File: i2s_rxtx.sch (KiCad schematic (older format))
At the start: 12 parts

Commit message: -- update
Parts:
- added C6, C8: 100nF, Capacitor_SMD:C_0805_2012Metric_Pad1.15x1.40mm_HandSolder, symbol agg:C
- added C7, C9: 10nF, Capacitor_SMD:C_0805_2012Metric_Pad1.15x1.40mm_HandSolder, symbol agg:C
- added IC2, IC3: AM26C31, agg:SOIC-16, symbol agg:AM26C31
- added J3: CONN_01x05, Connector_PinHeader_2.00mm:PinHeader_1x05_P2.00mm_Vertical, symbol agg:CONN_01x05
- added J4, J5: RJ45_Shielded, agg:RJ45_Weidmueller, symbol Connector:RJ45_Shielded
- C1: renamed from C?; footprint (none) -> Capacitor_SMD:CP_Elec_6.3x5.4
- C2, C3, C4, C5: renamed from C?; footprint (none) -> Capacitor_SMD:C_0805_2012Metric_Pad1.15x1.40mm_HandSolder
- J1: renamed from J?; footprint (none) -> Connector_PinHeader_2.00mm:PinHeader_1x02_P2.00mm_Vertical
- J2: renamed from J?; footprint (none) -> agg:RJ45_Weidmueller
- R1, R2, R4: renamed from R?; footprint (none) -> Resistor_SMD:R_1206_3216Metric_Pad1.42x1.75mm_HandSolder
- R3: renamed from R?; value 10=R -> 100R; footprint (none) -> Resistor_SMD:R_1206_3216Metric_Pad1.42x1.75mm_HandSolder
- gave numbers to parts that had none: 1
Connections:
- net +5V: now also C6.1, C7.1, C8.1, C9.1, IC2.16 (VCC), IC3.16 (VCC)
- net GND: now also C4.2, C5.2, IC1.8 (GND), C6.2, C7.2, C8.2, C9.2, IC2.12 (~G), IC2.4 (G), IC2.8 (GND), IC3.12 (~G), IC3.4 (G), IC3.8 (GND), J3.1, J4.SH, J5.SH
- net I2S_CH12: now also IC2.9 (3A), IC3.9 (3A), J3.4
- net I2S_CH34: now also IC2.15 (4A), IC3.15 (4A), J3.5
- net I2S_CLK: now also IC2.7 (2A), IC3.7 (2A), J3.3
- net I2S_WS: now also IC2.1 (1A), IC3.1 (1A), J3.2
- new net: IC2.10 (3Y), J4.5
- new net: IC2.11 (3Z), J4.6
- new net: IC2.13 (4Z), J4.8
- new net: IC2.14 (4Y), J4.7
- new net: IC2.2 (1Y), J4.1
- new net: IC2.3 (1Z), J4.2
- new net: IC2.5 (2Z), J4.4
- new net: IC2.6 (2Y), J4.3
- new net: IC3.10 (3Y), J5.5
- new net: IC3.11 (3Z), J5.6
- new net: IC3.13 (4Z), J5.8
- new net: IC3.14 (4Y), J5.7
- new net: IC3.2 (1Y), J5.1
- new net: IC3.3 (1Z), J5.2
- new net: IC3.5 (2Z), J5.4
- new net: IC3.6 (2Y), J5.3

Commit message: --update
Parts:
- added R5, R6, R7, R8: 500K, Resistor_SMD:R_0805_2012Metric_Pad1.15x1.40mm_HandSolder, symbol agg:R
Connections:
- net GND: now also R5.2, R6.2, R7.2, R8.2
- net I2S_CH12: now also R6.1
- net I2S_CH34: now also R5.1
- net I2S_CLK: now also R7.1
- net I2S_WS: now also R8.1
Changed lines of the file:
@@
 Text GLabel 2600 3400 0    50   Input ~ 0
 CH_34_Z
-Wire Wire Line
-	3450 1800 3500 1800
-Wire Wire Line
-	3450 2000 3500 2000
-Wire Wire Line
-	3450 2200 3500 2200
-Wire Wire Line
-	3450 2400 3500 2400
-Text GLabel 3500 1800 2    50   Input ~ 0
+Text GLabel 3950 1800 2    50   Input ~ 0
 I2S_WS
-Text GLabel 3500 2000 2    50   Input ~ 0
+Text GLabel 3950 2000 2    50   Input ~ 0
 I2S_CLK
-Text GLabel 3500 2200 2    50   Input ~ 0
+Text GLabel 3950 2200 2    50   Input ~ 0
 I2S_CH12
-Text GLabel 3500 2400 2    50   Input ~ 0
+Text GLabel 3950 2400 2    50   Input ~ 0
 I2S_CH34
 Wire Wire Line
@@
 $EndComp
 $Comp
-L power:GND #PWR?
+L power:GND #PWR0111
 U 1 1 5D0BFC09
 P 1050 2950
-F 0 "#PWR?" H 1050 2700 50  0001 C CNN
+F 0 "#PWR0111" H 1050 2700 50  0001 C CNN
 F 1 "GND" H 1055 2777 50  0000 C CNN
 F 2 "" H 1050 2950 50  0001 C CNN
@@
 Wire Wire Line
 	1050 2850 1050 2950
+$Comp
+L agg:R R5
+U 1 1 5D069D45
+P 3500 2450
+F 0 "R5" V 3504 2494 50  0000 L CNN
+F 1 "500K" V 3595 2494 50  0000 L CNN
+F 2 "Resistor_SMD:R_0805_2012Metric_Pad1.15x1.40mm_HandSolder" H 3500 2450 50  0001 C CNN
+F 3 "" H 3500 2450 50  0001 C CNN
+	1    3500 2450
+	0    1    1    0
+$EndComp
+$Comp
+L agg:R R6
+U 1 1 5D06AB9A
+P 3600 2250
+F 0 "R6" V 3604 2294 50  0000 L CNN
+F 1 "500K" V 3695 2294 50  0000 L CNN
+F 2 "Resistor_SMD:R_0805_2012Metric_Pad1.15x1.40mm_HandSolder" H 3600 2250 50  0001 C CNN
+F 3 "" H 3600 2250 50  0001 C CNN
+	1    3600 2250
+	0    1    1    0
+$EndComp
+$Comp
+L agg:R R7
+U 1 1 5D06B197
+P 3700 2050
+F 0 "R7" V 3704 2094 50  0000 L CNN
+F 1 "500K" V 3795 2094 50  0000 L CNN
+F 2 "Resistor_SMD:R_0805_2012Metric_Pad1.15x1.40mm_HandSolder" H 3700 2050 50  0001 C CNN
+F 3 "" H 3700 2050 50  0001 C CNN
+	1    3700 2050
+	0    1    1    0
+$EndComp
+$Comp
+L agg:R R8
+U 1 1 5D06B744
+P 3800 1850
+F 0 "R8" V 3804 1894 50  0000 L CNN
+F 1 "500K" V 3895 1894 50  0000 L CNN
+F 2 "Resistor_SMD:R_0805_2012Metric_Pad1.15x1.40mm_HandSolder" H 3800 1850 50  0001 C CNN
+F 3 "" H 3800 1850 50  0001 C CNN
+	1    3800 1850
+	0    1    1    0
+$EndComp
+Wire Wire Line
+	3450 1800 3800 1800
+Wire Wire Line
+	3800 1800 3950 1800
+Connection ~ 3800 1800
+Wire Wire Line
+	3600 2600 3500 2600
+Connection ~ 3600 2600
+$Comp
+L power:GND #PWR0112
+U 1 1 5D0A366B
+P 3600 2700
+F 0 "#PWR0112" H 3600 2450 50  0001 C CNN
+F 1 "GND" H 3605 2527 50  0000 C CNN
+F 2 "" H 3600 2700 50  0001 C CNN
+F 3 "" H 3600 2700 50  0001 C CNN
+	1    3600 2700
+	1    0    0    -1
+$EndComp
+Wire Wire Line
+	3600 2600 3600 2700
+Wire Wire Line
+	3600 2600 3700 2600
+Wire Wire Line
+	3800 1800 3800 1850
+Wire Wire Line
+	3450 2400 3500 2400
+Wire Wire Line
+	3450 2000 3700 2000
+Wire Wire Line
+	3450 2200 3600 2200
+Wire Wire Line
+	3700 2000 3700 2050
+Connection ~ 3700 2000
+Wire Wire Line
+	3700 2000 3950 2000
+Wire Wire Line
+	3600 2200 3600 2250
+Connection ~ 3600 2200
+Wire Wire Line
+	3600 2200 3950 2200
+Wire Wire Line
+	3500 2400 3500 2450
+Connection ~ 3500 2400
+Wire Wire Line
+	3500 2400 3950 2400
+Wire Wire Line
+	3500 2550 3500 2600
+Wire Wire Line
+	3600 2350 3600 2600
+Wire Wire Line
+	3700 2150 3700 2600
+Connection ~ 3700 2600
+Wire Wire Line
+	3700 2600 3800 2600
+Wire Wire Line
+	3800 1950 3800 2600
 $EndSCHEMATC

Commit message: -- added mounting holes
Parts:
- added H1, H2, H3, H4: MountingHole, MountingHole:MountingHole_3.2mm_M3_Pad, symbol Mechanical:MountingHole
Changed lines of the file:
@@
 Wire Wire Line
 	3800 1950 3800 2600
+$Comp
+L Mechanical:MountingHole H1
+U 1 1 5D0E85FD
+P 850 3500
+F 0 "H1" H 950 3546 50  0000 L CNN
+F 1 "MountingHole" H 950 3455 50  0000 L CNN
+F 2 "MountingHole:MountingHole_3.2mm_M3_Pad" H 850 3500 50  0001 C CNN
+F 3 "~" H 850 3500 50  0001 C CNN
+	1    850  3500
+	1    0    0    -1
+$EndComp
+$Comp
+L Mechanical:MountingHole H2
+U 1 1 5D0E907F
+P 850 3700
+F 0 "H2" H 950 3746 50  0000 L CNN
+F 1 "MountingHole" H 950 3655 50  0000 L CNN
+F 2 "MountingHole:MountingHole_3.2mm_M3_Pad" H 850 3700 50  0001 C CNN
+F 3 "~" H 850 3700 50  0001 C CNN
+	1    850  3700
+	1    0    0    -1
+$EndComp
+$Comp
+L Mechanical:MountingHole H3
+U 1 1 5D0E92F0
+P 850 3900
+F 0 "H3" H 950 3946 50  0000 L CNN
+F 1 "MountingHole" H 950 3855 50  0000 L CNN
+F 2 "MountingHole:MountingHole_3.2mm_M3_Pad" H 850 3900 50  0001 C CNN
+F 3 "~" H 850 3900 50  0001 C CNN
+	1    850  3900
+	1    0    0    -1
+$EndComp
+$Comp
+L Mechanical:MountingHole H4
+U 1 1 5D0E9AAA
+P 850 4100
+F 0 "H4" H 950 4146 50  0000 L CNN
+F 1 "MountingHole" H 950 4055 50  0000 L CNN
+F 2 "MountingHole:MountingHole_3.2mm_M3_Pad" H 850 4100 50  0001 C CNN
+F 3 "~" H 850 4100 50  0001 C CNN
+	1    850  4100
+	1    0    0    -1
+$EndComp
 $EndSCHEMATC

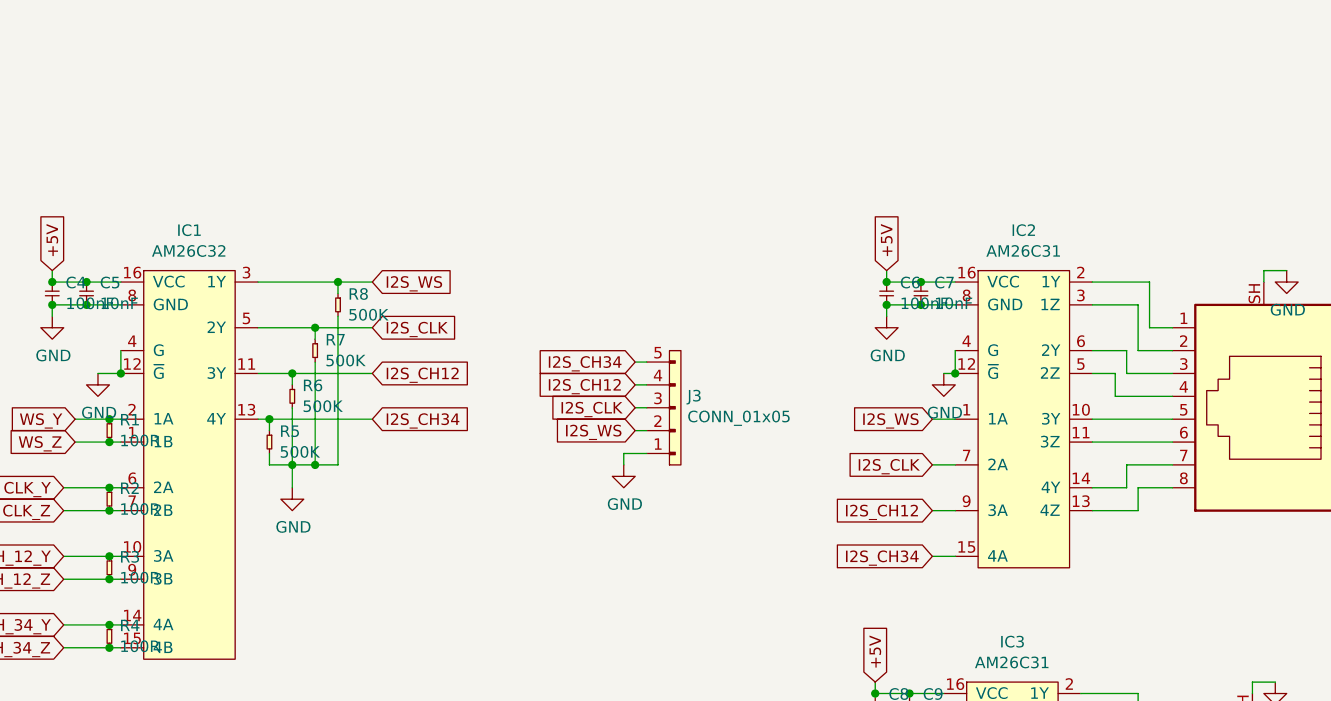
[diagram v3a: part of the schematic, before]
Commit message: -- added voltage divider for 3.3V outputs
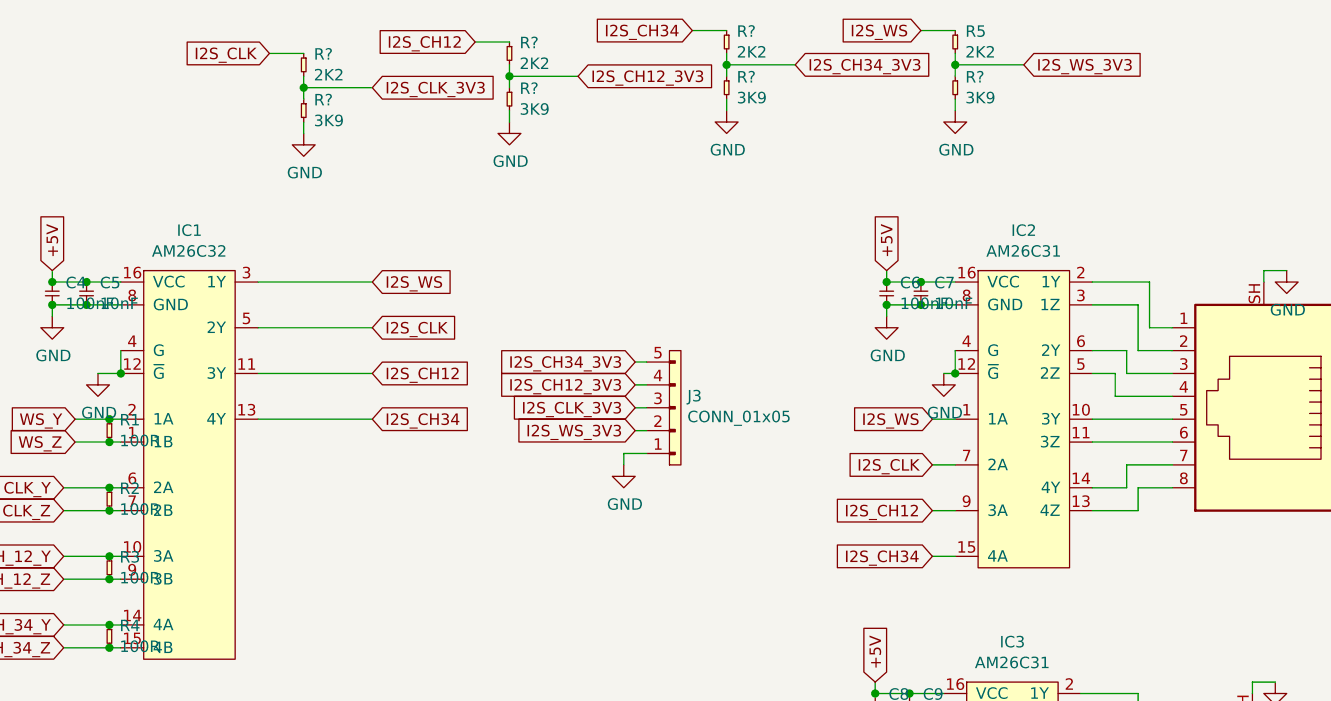
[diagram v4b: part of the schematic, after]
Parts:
- removed R6, R7, R8: 500K, Resistor_SMD:R_0805_2012Metric_Pad1.15x1.40mm_HandSolder, symbol agg:R
- added R? (x4): 3K9, Resistor_SMD:R_0805_2012Metric_Pad1.15x1.40mm_HandSolder, symbol agg:R
- added R? (x3): 2K2, Resistor_SMD:R_0805_2012Metric_Pad1.15x1.40mm_HandSolder, symbol agg:R
- R5: value 500K -> 2K2
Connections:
- net GND: now also R?.2, R?.2, R?.2, R?.2; no longer R5.2
- net I2S_CH12: now also R?.1; no longer J3.4
- net I2S_CH34: now also R?.1; no longer J3.5, R5.1
- net I2S_CLK: now also R?.1; no longer J3.3
- net I2S_WS: now also R5.1; no longer J3.2
- new net I2S_CH12_3V3: J3.4, R?.1, R?.2
- new net I2S_CH34_3V3: J3.5, R?.1, R?.2
- new net I2S_CLK_3V3: J3.3, R?.1, R?.2
- new net I2S_WS_3V3: J3.2, R5.2, R?.1
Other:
- moved on the sheet: R5
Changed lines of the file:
@@
 	5050 2550 5150 2550
 Text GLabel 5100 2450 0    50   Input ~ 0
-I2S_WS
+I2S_WS_3V3
 Text GLabel 5100 2350 0    50   Input ~ 0
-I2S_CLK
+I2S_CLK_3V3
 Text GLabel 5100 2250 0    50   Input ~ 0
-I2S_CH12
+I2S_CH12_3V3
 Text GLabel 5100 2150 0    50   Input ~ 0
-I2S_CH34
+I2S_CH34_3V3
 Wire Wire Line
 	6200 1900 6200 1950
@@
 L agg:R R5
 U 1 1 5D069D45
-P 3500 2450
-F 0 "R5" V 3504 2494 50  0000 L CNN
-F 1 "500K" V 3595 2494 50  0000 L CNN
-F 2 "Resistor_SMD:R_0805_2012Metric_Pad1.15x1.40mm_HandSolder" H 3500 2450 50  0001 C CNN
-F 3 "" H 3500 2450 50  0001 C CNN
-	1    3500 2450
-	0    1    1    0
-$EndComp
-$Comp
-L agg:R R6
-U 1 1 5D06AB9A
-P 3600 2250
-F 0 "R6" V 3604 2294 50  0000 L CNN
-F 1 "500K" V 3695 2294 50  0000 L CNN
-F 2 "Resistor_SMD:R_0805_2012Metric_Pad1.15x1.40mm_HandSolder" H 3600 2250 50  0001 C CNN
-F 3 "" H 3600 2250 50  0001 C CNN
-	1    3600 2250
-	0    1    1    0
-$EndComp
-$Comp
-L agg:R R7
-U 1 1 5D06B197
-P 3700 2050
-F 0 "R7" V 3704 2094 50  0000 L CNN
-F 1 "500K" V 3795 2094 50  0000 L CNN
-F 2 "Resistor_SMD:R_0805_2012Metric_Pad1.15x1.40mm_HandSolder" H 3700 2050 50  0001 C CNN
-F 3 "" H 3700 2050 50  0001 C CNN
-	1    3700 2050
-	0    1    1    0
-$EndComp
-$Comp
-L agg:R R8
-U 1 1 5D06B744
-P 3800 1850
-F 0 "R8" V 3804 1894 50  0000 L CNN
-F 1 "500K" V 3895 1894 50  0000 L CNN
-F 2 "Resistor_SMD:R_0805_2012Metric_Pad1.15x1.40mm_HandSolder" H 3800 1850 50  0001 C CNN
-F 3 "" H 3800 1850 50  0001 C CNN
-	1    3800 1850
-	0    1    1    0
-$EndComp
-Wire Wire Line
-	3450 1800 3800 1800
-Wire Wire Line
-	3800 1800 3950 1800
-Connection ~ 3800 1800
-Wire Wire Line
-	3600 2600 3500 2600
-Connection ~ 3600 2600
-$Comp
-L power:GND #PWR0112
-U 1 1 5D0A366B
-P 3600 2700
-F 0 "#PWR0112" H 3600 2450 50  0001 C CNN
-F 1 "GND" H 3605 2527 50  0000 C CNN
-F 2 "" H 3600 2700 50  0001 C CNN
-F 3 "" H 3600 2700 50  0001 C CNN
-	1    3600 2700
-	1    0    0    -1
-$EndComp
-Wire Wire Line
-	3600 2600 3600 2700
-Wire Wire Line
-	3600 2600 3700 2600
-Wire Wire Line
-	3800 1800 3800 1850
-Wire Wire Line
-	3450 2400 3500 2400
-Wire Wire Line
-	3450 2000 3700 2000
-Wire Wire Line
-	3450 2200 3600 2200
-Wire Wire Line
-	3700 2000 3700 2050
-Connection ~ 3700 2000
-Wire Wire Line
-	3700 2000 3950 2000
-Wire Wire Line
-	3600 2200 3600 2250
-Connection ~ 3600 2200
-Wire Wire Line
-	3600 2200 3950 2200
-Wire Wire Line
-	3500 2400 3500 2450
-Connection ~ 3500 2400
-Wire Wire Line
-	3500 2400 3950 2400
-Wire Wire Line
-	3500 2550 3500 2600
-Wire Wire Line
-	3600 2350 3600 2600
-Wire Wire Line
-	3700 2150 3700 2600
-Connection ~ 3700 2600
-Wire Wire Line
-	3700 2600 3800 2600
-Wire Wire Line
-	3800 1950 3800 2600
+P 6500 700
+F 0 "R5" V 6504 744 50  0000 L CNN
+F 1 "2K2" V 6595 744 50  0000 L CNN
+F 2 "Resistor_SMD:R_0805_2012Metric_Pad1.15x1.40mm_HandSolder" H 6500 700 50  0001 C CNN
+F 3 "" H 6500 700 50  0001 C CNN
+	1    6500 700
+	0    1    1    0
+$EndComp
 $Comp
 L Mechanical:MountingHole H1
@@
 	1    0    0    -1
 $EndComp
+Wire Wire Line
+	3450 2400 3950 2400
+Wire Wire Line
+	3450 2200 3950 2200
+Wire Wire Line
+	3450 2000 3950 2000
+Wire Wire Line
+	3450 1800 3950 1800
+Text GLabel 6350 700  0    50   Input ~ 0
+I2S_WS
+$Comp
+L agg:R R?
+U 1 1 5D540B22
+P 6500 900
+F 0 "R?" V 6504 944 50  0000 L CNN
+F 1 "3K9" V 6595 944 50  0000 L CNN
+F 2 "Resistor_SMD:R_0805_2012Metric_Pad1.15x1.40mm_HandSolder" H 6500 900 50  0001 C CNN
+F 3 "" H 6500 900 50  0001 C CNN
+	1    6500 900
+	0    1    1    0
+$EndComp
+$Comp
+L power:GND #PWR?
+U 1 1 5D54109E
+P 6500 1050
+F 0 "#PWR?" H 6500 800 50  0001 C CNN
+F 1 "GND" H 6505 877 50  0000 C CNN
+F 2 "" H 6500 1050 50  0001 C CNN
+F 3 "" H 6500 1050 50  0001 C CNN
+	1    6500 1050
+	1    0    0    -1
+$EndComp
+Wire Wire Line
+	6350 700  6500 700
+Wire Wire Line
+	6500 800  6500 850
+Text GLabel 6800 850  2    50   Input ~ 0
+I2S_WS_3V3
+Wire Wire Line
+	6800 850  6500 850
+Wire Wire Line
+	6500 1000 6500 1050
+Wire Wire Line
+	6500 900  6500 850
+Connection ~ 6500 850
+$Comp
+L agg:R R?
+U 1 1 5D56E9E4
+P 3650 800
+F 0 "R?" V 3654 844 50  0000 L CNN
+F 1 "2K2" V 3745 844 50  0000 L CNN
+F 2 "Resistor_SMD:R_0805_2012Metric_Pad1.15x1.40mm_HandSolder" H 3650 800 50  0001 C CNN
+F 3 "" H 3650 800 50  0001 C CNN
+	1    3650 800
+	0    1    1    0
+$EndComp
+Text GLabel 3500 800  0    50   Input ~ 0
+I2S_CLK
+$Comp
+L agg:R R?
+U 1 1 5D56E9EF
+P 3650 1000
+F 0 "R?" V 3654 1044 50  0000 L CNN
+F 1 "3K9" V 3745 1044 50  0000 L CNN
+F 2 "Resistor_SMD:R_0805_2012Metric_Pad1.15x1.40mm_HandSolder" H 3650 1000 50  0001 C CNN
+F 3 "" H 3650 1000 50  0001 C CNN
+	1    3650 1000
+	0    1    1    0
+$EndComp
+$Comp
+L power:GND #PWR?
+U 1 1 5D56E9F9
+P 3650 1150
+F 0 "#PWR?" H 3650 900 50  0001 C CNN
+F 1 "GND" H 3655 977 50  0000 C CNN
+F 2 "" H 3650 1150 50  0001 C CNN
+F 3 "" H 3650 1150 50  0001 C CNN
+	1    3650 1150
+	1    0    0    -1
+$EndComp
+Wire Wire Line
+	3500 800  3650 800
+Wire Wire Line
+	3650 900  3650 950
+Text GLabel 3950 950  2    50   Input ~ 0
+I2S_CLK_3V3
+Wire Wire Line
+	3950 950  3650 950
+Wire Wire Line
+	3650 1100 3650 1150
+Wire Wire Line
+	3650 1000 3650 950
+Connection ~ 3650 950
+$Comp
+L agg:R R?
+U 1 1 5D5754C4
+P 4550 750
+F 0 "R?" V 4554 794 50  0000 L CNN
+F 1 "2K2" V 4645 794 50  0000 L CNN
+F 2 "Resistor_SMD:R_0805_2012Metric_Pad1.15x1.40mm_HandSolder" H 4550 750 50  0001 C CNN
+F 3 "" H 4550 750 50  0001 C CNN
+	1    4550 750
+	0    1    1    0
+$EndComp
+Text GLabel 4400 750  0    50   Input ~ 0
+I2S_CH12
+$Comp
+L agg:R R?
+U 1 1 5D5754CF
+P 4550 950
+F 0 "R?" V 4554 994 50  0000 L CNN
+F 1 "3K9" V 4645 994 50  0000 L CNN
+F 2 "Resistor_SMD:R_0805_2012Metric_Pad1.15x1.40mm_HandSolder" H 4550 950 50  0001 C CNN
+F 3 "" H 4550 950 50  0001 C CNN
+	1    4550 950
+	0    1    1    0
+$EndComp
+$Comp
+L power:GND #PWR?
+U 1 1 5D5754D9
+P 4550 1100
+F 0 "#PWR?" H 4550 850 50  0001 C CNN
+F 1 "GND" H 4555 927 50  0000 C CNN
+F 2 "" H 4550 1100 50  0001 C CNN
+F 3 "" H 4550 1100 50  0001 C CNN
+	1    4550 1100
+	1    0    0    -1
+$EndComp
+Wire Wire Line
+	4400 750  4550 750
+Wire Wire Line
+	4550 850  4550 900
+Text GLabel 4850 900  2    50   Input ~ 0
+I2S_CH12_3V3
+Wire Wire Line
+	4850 900  4550 900
+Wire Wire Line
+	4550 1050 4550 1100
+Wire Wire Line
+	4550 950  4550 900
+Connection ~ 4550 900
+$Comp
+L agg:R R?
+U 1 1 5D57D61F
+P 5500 700
+F 0 "R?" V 5504 744 50  0000 L CNN
+F 1 "2K2" V 5595 744 50  0000 L CNN
+F 2 "Resistor_SMD:R_0805_2012Metric_Pad1.15x1.40mm_HandSolder" H 5500 700 50  0001 C CNN
+F 3 "" H 5500 700 50  0001 C CNN
+	1    5500 700
+	0    1    1    0
+$EndComp
+Text GLabel 5350 700  0    50   Input ~ 0
+I2S_CH34
+$Comp
+L agg:R R?
+U 1 1 5D57D62A
+P 5500 900
+F 0 "R?" V 5504 944 50  0000 L CNN
+F 1 "3K9" V 5595 944 50  0000 L CNN
+F 2 "Resistor_SMD:R_0805_2012Metric_Pad1.15x1.40mm_HandSolder" H 5500 900 50  0001 C CNN
+F 3 "" H 5500 900 50  0001 C CNN
+	1    5500 900
+	0    1    1    0
+$EndComp
+$Comp
+L power:GND #PWR?
+U 1 1 5D57D634
+P 5500 1050
+F 0 "#PWR?" H 5500 800 50  0001 C CNN
+F 1 "GND" H 5505 877 50  0000 C CNN
+F 2 "" H 5500 1050 50  0001 C CNN
+F 3 "" H 5500 1050 50  0001 C CNN
+	1    5500 1050
+	1    0    0    -1
+$EndComp
+Wire Wire Line
+	5350 700  5500 700
+Wire Wire Line
+	5500 800  5500 850
+Text GLabel 5800 850  2    50   Input ~ 0
+I2S_CH34_3V3
+Wire Wire Line
+	5800 850  5500 850
+Wire Wire Line
+	5500 1000 5500 1050
+Wire Wire Line
+	5500 900  5500 850
+Connection ~ 5500 850
 $EndSCHEMATC
